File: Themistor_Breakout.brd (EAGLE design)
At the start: 160 x 100 mm, 8 parts

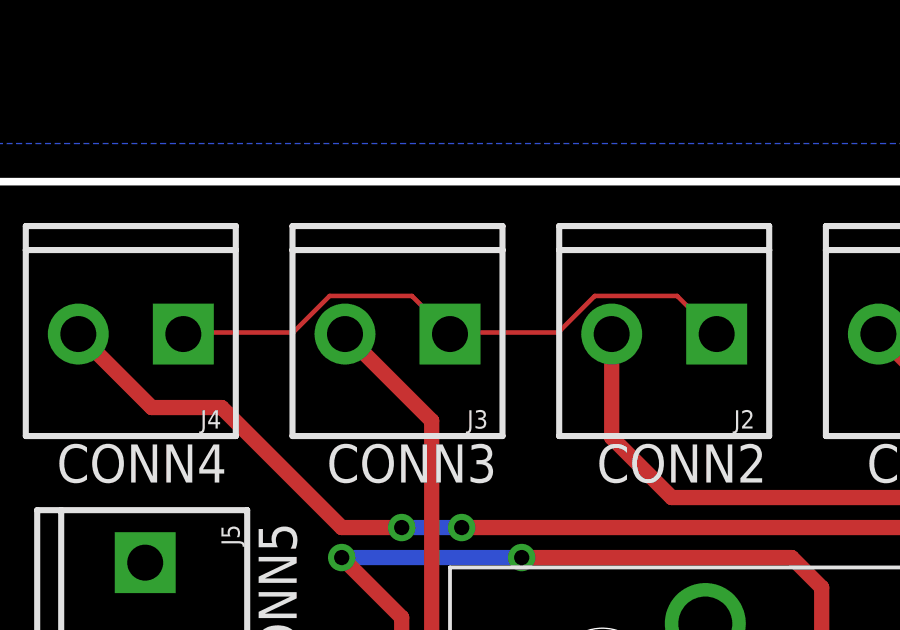
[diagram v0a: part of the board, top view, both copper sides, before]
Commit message: Removed stray gnd traces from autorouter
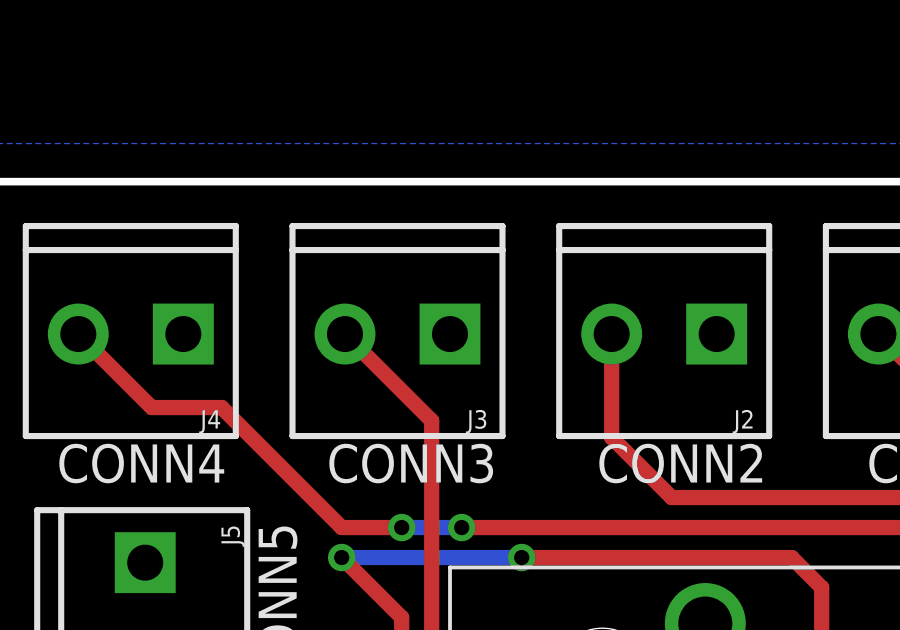
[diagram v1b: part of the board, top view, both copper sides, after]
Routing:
- net GND: track 19.9 -> 0.00 mm
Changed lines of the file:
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@@
 <contactref element="J6" pad="1"/>
 <contactref element="J7" pad="1"/>
-<wire x1="58.2168" y1="44.5008" x2="54.7116" y2="44.5008" width="0.1524" layer="1"/>
-<wire x1="59.436" y1="45.72" x2="58.2168" y2="44.5008" width="0.1524" layer="1"/>
-<wire x1="62.1792" y1="45.72" x2="59.436" y2="45.72" width="0.1524" layer="1"/>
-<wire x1="63.3984" y1="44.5008" x2="62.1792" y2="45.72" width="0.1524" layer="1"/>
-<wire x1="54.7116" y1="44.5008" x2="54.61" y2="44.45" width="0.1524" layer="1"/>
-<wire x1="63.3984" y1="44.5008" x2="63.5" y2="44.45" width="0.1524" layer="1"/>
-<wire x1="49.3776" y1="44.5008" x2="45.72" y2="44.5008" width="0.1524" layer="1"/>
-<wire x1="50.5968" y1="45.72" x2="49.3776" y2="44.5008" width="0.1524" layer="1"/>
-<wire x1="53.34" y1="45.72" x2="50.5968" y2="45.72" width="0.1524" layer="1"/>
-<wire x1="54.61" y1="44.45" x2="53.34" y2="45.72" width="0.1524" layer="1"/>
-<wire x1="45.72" y1="44.5008" x2="45.72" y2="44.45" width="0.1524" layer="1"/>
 <polygon width="0.254" layer="16">
 <vertex x="38.1" y="50.8"/>

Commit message: Added mounting holes to thermistor breakout
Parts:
- added H1, H2: MOUNT-PAD-ROUND3.6, holes:3,6-PAD
- moved J5 5.08 mm to (39.4, 36.8)
- moved J6 5.08 mm to (39.4, 27.9)
- moved J7 5.08 mm to (39.4, 19.1)
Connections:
- net GND: now also H1.B3,6, H2.B3,6
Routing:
- net ETH7: track 30.0 -> 35.0 mm
- net ETH5: track 21.5 -> 26.6 mm
- net ETH6: track 44.1 -> 48.6 mm, vias 2 -> 3
- net ETH4: track 48.8 -> 51.2 mm
- added copper zone on layer 1, net GND
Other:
- outline, holes or cut-outs redrawn
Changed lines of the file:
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@@
 <wire x1="160" y1="100" x2="0" y2="100" width="0" layer="20"/>
 <wire x1="0" y1="100" x2="0" y2="0" width="0" layer="20"/>
-<wire x1="39.37" y1="49.53" x2="39.37" y2="11.43" width="0.254" layer="20"/>
-<wire x1="39.37" y1="11.43" x2="71.12" y2="11.43" width="0.254" layer="20"/>
-<wire x1="71.12" y1="11.43" x2="76.2" y2="16.51" width="0.254" layer="20"/>
-<wire x1="76.2" y1="16.51" x2="76.2" y2="49.53" width="0.254" layer="20"/>
-<wire x1="76.2" y1="49.53" x2="39.37" y2="49.53" width="0.254" layer="20"/>
+<wire x1="34.29" y1="49.53" x2="34.29" y2="11.43" width="0.254" layer="20"/>
+<wire x1="34.29" y1="11.43" x2="64.516" y2="11.43" width="0.254" layer="20"/>
+<wire x1="76.2" y1="9.906" x2="76.2" y2="49.53" width="0.254" layer="20"/>
+<wire x1="76.2" y1="49.53" x2="34.29" y2="49.53" width="0.254" layer="20"/>
 <text x="41.5" y="39.5" size="1.27" layer="21" font="vector" ratio="15">CONN4</text>
 <text x="50.5" y="39.5" size="1.27" layer="21" font="vector" ratio="15">CONN3</text>
 <text x="59.5" y="39.5" size="1.27" layer="21" font="vector" ratio="15">CONN2</text>
 <text x="68.5" y="39.5" size="1.27" layer="21" font="vector" ratio="15">CONN1</text>
-<text x="49.5" y="32.5" size="1.27" layer="21" font="vector" ratio="15" rot="R90">CONN5</text>
-<text x="49.5" y="23.5" size="1.27" layer="21" font="vector" ratio="15" rot="R90">CONN6</text>
-<text x="49.5" y="14.5" size="1.27" layer="21" font="vector" ratio="15" rot="R90">CONN7</text>
+<text x="44.42" y="32.5" size="1.27" layer="21" font="vector" ratio="15" rot="R90">CONN5</text>
+<text x="44.42" y="23.5" size="1.27" layer="21" font="vector" ratio="15" rot="R90">CONN6</text>
+<text x="44.42" y="14.5" size="1.27" layer="21" font="vector" ratio="15" rot="R90">CONN7</text>
+<wire x1="76.2" y1="9.906" x2="72.644" y2="6.35" width="0.254" layer="20"/>
+<wire x1="72.644" y1="6.35" x2="69.596" y2="6.35" width="0.254" layer="20"/>
+<wire x1="69.596" y1="6.35" x2="64.516" y2="11.43" width="0.254" layer="20"/>
 </plain>
 <attributes>
@@
 <attribute name="PROD_ID" value="CONN-08399" x="45.72" y="44.45" size="1.778" layer="27" font="vector" ratio="15" rot="R180" display="off"/>
 </element>
-<element name="J5" library="SparkFun-Connectors" library_urn="urn:adsk.eagle:library:513" package="SCREWTERMINAL-3.5MM-2" package3d_urn="urn:adsk.eagle:package:38050/1" value="" x="44.45" y="36.83" rot="R270">
-<attribute name="PROD_ID" value="CONN-08399" x="44.45" y="36.83" size="1.778" layer="27" font="vector" ratio="15" rot="R270" display="off"/>
-</element>
-<element name="J6" library="SparkFun-Connectors" library_urn="urn:adsk.eagle:library:513" package="SCREWTERMINAL-3.5MM-2" package3d_urn="urn:adsk.eagle:package:38050/1" value="" x="44.45" y="27.94" rot="R270">
-<attribute name="PROD_ID" value="CONN-08399" x="44.45" y="27.94" size="1.778" layer="27" font="vector" ratio="15" rot="R270" display="off"/>
-</element>
-<element name="J7" library="SparkFun-Connectors" library_urn="urn:adsk.eagle:library:513" package="SCREWTERMINAL-3.5MM-2" package3d_urn="urn:adsk.eagle:package:38050/1" value="" x="44.45" y="19.05" rot="R270">
-<attribute name="PROD_ID" value="CONN-08399" x="44.45" y="19.05" size="1.778" layer="27" font="vector" ratio="15" rot="R270" display="off"/>
-</element>
+<element name="J5" library="SparkFun-Connectors" library_urn="urn:adsk.eagle:library:513" package="SCREWTERMINAL-3.5MM-2" package3d_urn="urn:adsk.eagle:package:38050/1" value="" x="39.37" y="36.83" rot="R270">
+<attribute name="PROD_ID" value="CONN-08399" x="39.37" y="36.83" size="1.778" layer="27" font="vector" ratio="15" rot="R270" display="off"/>
+</element>
+<element name="J6" library="SparkFun-Connectors" library_urn="urn:adsk.eagle:library:513" package="SCREWTERMINAL-3.5MM-2" package3d_urn="urn:adsk.eagle:package:38050/1" value="" x="39.37" y="27.94" rot="R270">
+<attribute name="PROD_ID" value="CONN-08399" x="39.37" y="27.94" size="1.778" layer="27" font="vector" ratio="15" rot="R270" display="off"/>
+</element>
+<element name="J7" library="SparkFun-Connectors" library_urn="urn:adsk.eagle:library:513" package="SCREWTERMINAL-3.5MM-2" package3d_urn="urn:adsk.eagle:package:38050/1" value="" x="39.37" y="19.05" rot="R270">
+<attribute name="PROD_ID" value="CONN-08399" x="39.37" y="19.05" size="1.778" layer="27" font="vector" ratio="15" rot="R270" display="off"/>
+</element>
+<element name="H1" library="holes" library_urn="urn:adsk.eagle:library:237" package="3,6-PAD" package3d_urn="urn:adsk.eagle:package:14284/1" value="MOUNT-PAD-ROUND3.6" x="71.12" y="11.43"/>
+<element name="H2" library="holes" library_urn="urn:adsk.eagle:library:237" package="3,6-PAD" package3d_urn="urn:adsk.eagle:package:14284/1" value="MOUNT-PAD-ROUND3.6" x="49.276" y="28.702"/>
 </elements>
 <signals>
@@
 <contactref element="J6" pad="1"/>
 <contactref element="J7" pad="1"/>
+<contactref element="H2" pad="B3,6"/>
+<contactref element="H1" pad="B3,6"/>
+<via x="57.15" y="39.624" extent="1-16" drill="0.35"/>
+<via x="38.1" y="43.18" extent="1-16" drill="0.35"/>
+<via x="68.58" y="27.94" extent="1-16" drill="0.35"/>
+<polygon width="0.254" layer="1">
+<vertex x="33.02" y="50.8"/>
+<vertex x="33.02" y="10.16"/>
+<vertex x="63.5" y="10.16"/>
+<vertex x="68.58" y="5.08"/>
+<vertex x="73.66" y="5.08"/>
+<vertex x="77.724" y="9.144"/>
+<vertex x="77.724" y="49.276"/>
+<vertex x="76.2" y="50.8"/>
+</polygon>
 <polygon width="0.254" layer="16">
-<vertex x="38.1" y="50.8"/>
-<vertex x="38.1" y="10.16"/>
-<vertex x="71.882" y="10.16"/>
-<vertex x="77.47" y="15.748"/>
-<vertex x="77.47" y="50.8"/>
+<vertex x="33.02" y="10.16"/>
+<vertex x="63.5" y="10.16"/>
+<vertex x="68.58" y="5.08"/>
+<vertex x="73.406" y="5.08"/>
+<vertex x="77.47" y="9.144"/>
+<vertex x="77.47" y="49.53"/>
+<vertex x="76.2" y="50.8"/>
+<vertex x="34.29" y="50.8"/>
+<vertex x="33.02" y="49.53"/>
 </polygon>
+<via x="50.8" y="17.78" extent="1-16" drill="0.35"/>
+<via x="53.34" y="25.4" extent="1-16" drill="0.35"/>
+<via x="45.72" y="25.4" extent="1-16" drill="0.35"/>
+<via x="73.66" y="22.86" extent="1-16" drill="0.35"/>
+<via x="50.8" y="35.56" extent="1-16" drill="0.35"/>
 </signal>
 <signal name="ETH7">
@@
 <via x="55" y="27" extent="1-16" drill="0.508"/>
 <wire x1="55" y1="27" x2="55" y2="17" width="0.508" layer="1"/>
-<wire x1="53.55" y1="15.55" x2="44.45" y2="15.55" width="0.508" layer="1"/>
+<wire x1="53.55" y1="15.55" x2="39.37" y2="15.55" width="0.508" layer="1"/>
 <wire x1="55" y1="17" x2="53.55" y2="15.55" width="0.508" layer="1"/>
 </signal>
@@
 <contactref element="ETH1" pad="P$6"/>
 <contactref element="J6" pad="2"/>
-<wire x1="64.01" y1="28.19" x2="67" y2="31.18" width="0.508" layer="1"/>
-<wire x1="67" y1="31.18" x2="67" y2="36" width="0.508" layer="1"/>
-<wire x1="67" y1="36" x2="66" y2="37" width="0.508" layer="1"/>
-<wire x1="66" y1="37" x2="57" y2="37" width="0.508" layer="1"/>
-<via x="57" y="37" extent="1-16" drill="0.508"/>
-<wire x1="57" y1="37" x2="51" y2="37" width="0.508" layer="16"/>
-<via x="51" y="37" extent="1-16" drill="0.508"/>
-<wire x1="51" y1="37" x2="53" y2="35" width="0.508" layer="1"/>
-<wire x1="53" y1="35" x2="53" y2="30" width="0.508" layer="1"/>
-<wire x1="53" y1="30" x2="47.44" y2="24.44" width="0.508" layer="1"/>
-<wire x1="47.44" y1="24.44" x2="44.45" y2="24.44" width="0.508" layer="1"/>
+<wire x1="39.37" y1="24.44" x2="40.95" y2="22.86" width="0.508" layer="1"/>
+<wire x1="40.95" y1="22.86" x2="46.99" y2="22.86" width="0.508" layer="1"/>
+<via x="46.99" y="22.86" extent="1-16" drill="0.35"/>
+<wire x1="46.99" y1="22.86" x2="56.388" y2="22.86" width="0.508" layer="16"/>
+<via x="56.388" y="22.86" extent="1-16" drill="0.35"/>
+<wire x1="56.388" y1="22.86" x2="56.388" y2="17.272" width="0.508" layer="1"/>
+<wire x1="56.388" y1="17.272" x2="58.42" y2="15.24" width="0.508" layer="1"/>
+<wire x1="58.42" y1="15.24" x2="66.04" y2="15.24" width="0.508" layer="1"/>
+<wire x1="66.04" y1="15.24" x2="66.04" y2="20.32" width="0.508" layer="1"/>
+<via x="66.04" y="20.32" extent="1-16" drill="0.35"/>
+<wire x1="66.04" y1="20.32" x2="66.04" y2="27.94" width="0.508" layer="16"/>
+<wire x1="66.04" y1="27.94" x2="65.79" y2="28.19" width="0.508" layer="16"/>
+<wire x1="65.79" y1="28.19" x2="64.01" y2="28.19" width="0.508" layer="16"/>
 </signal>
 <signal name="ETH5">
@@
 <wire x1="62.23" y1="27.17" x2="58.83" y2="27.17" width="0.508" layer="1"/>
 <via x="55" y="33" extent="1-16" drill="0.508"/>
-<wire x1="55" y1="33" x2="52" y2="33" width="0.508" layer="16"/>
-<via x="52" y="33" extent="1-16" drill="0.508"/>
-<wire x1="52" y1="33" x2="44.78" y2="33" width="0.508" layer="1"/>
-<wire x1="44.78" y1="33" x2="44.45" y2="33.33" width="0.508" layer="1"/>
+<wire x1="55" y1="33" x2="46.92" y2="33" width="0.508" layer="16"/>
+<via x="46.92" y="33" extent="1-16" drill="0.508"/>
+<wire x1="46.92" y1="33" x2="39.7" y2="33" width="0.508" layer="1"/>
+<wire x1="39.7" y1="33" x2="39.37" y2="33.33" width="0.508" layer="1"/>
 <wire x1="55" y1="31" x2="55" y2="33" width="0.508" layer="1"/>
 <wire x1="58.83" y1="27.17" x2="55" y2="31" width="0.508" layer="1"/>
@@
 <wire x1="55" y1="38" x2="53" y2="38" width="0.508" layer="16"/>
 <via x="53" y="38" extent="1-16" drill="0.508"/>
-<wire x1="53" y1="38" x2="51" y2="38" width="0.508" layer="1"/>
+<wire x1="53" y1="38" x2="46.936" y2="38" width="0.508" layer="1"/>
 <wire x1="47" y1="42" x2="44.67" y2="42" width="0.508" layer="1"/>
 <wire x1="44.67" y1="42" x2="42.22" y2="44.45" width="0.508" layer="1"/>
-<wire x1="51" y1="38" x2="47" y2="42" width="0.508" layer="1"/>
+<wire x1="46.936" y1="38" x2="47" y2="42" width="0.508" layer="1"/>
 </signal>
 <signal name="ETH3">
@@
 <wire x1="71.34" y1="42" x2="68.89" y2="44.45" width="0.508" layer="1"/>
 </signal>
+<signal name="N$10">
+<via x="66.04" y="33.02" extent="1-16" drill="0.35"/>
+</signal>
 </signals>

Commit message: Remade thermistor breakout gerbers
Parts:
- moved H2 33.4 mm to (16.3, 23.6)
- moved J1 33.4 mm to (39.4, 39.4)
- moved ETH1 33.4 mm to (26.7, 21.6)
- moved H1 33.4 mm to (38.1, 6.35)
- moved J2 33.4 mm to (30.5, 39.4)
- moved J3 33.4 mm to (21.6, 39.4)
- moved J4 33.4 mm to (12.7, 39.4)
- moved J6 33.4 mm to (6.35, 22.9)
- moved J5 33.4 mm to (6.35, 31.8)
- moved J7 33.4 mm to (6.35, 14.0)
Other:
- board size 160 x 100 mm -> 41.9 x 43.2 mm
